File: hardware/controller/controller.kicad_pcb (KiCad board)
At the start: 4 copper layers, 80 x 100 mm, 70 parts, among them J1 TYPE-C 16PLT-H10.0, J2 TYPE-C 16PLT-H10.0, SW1 EVP-ASAC1A, SW2 CL-SB-13A-02T, SW3 EVP-ASAC1A, SW4 EVP-ASAC1A, SW5 EVP-ASAC1A, SW6 EVP-ASAC1A, U1 ZX-PM2.54-1-16PY, U10 XDJK-0051-025, U2 ZX-PM2.54-1-16PY, U3 ZX-PM2.54-1-16PY, U4 ZX-PM2.54-1-16PY, U5 SN74LVC1T45DBV, U6 SN74LVC1T45DBV, U7 EA8212HT6R, U8 EA8212HT6R, U9 EA8212HT6R

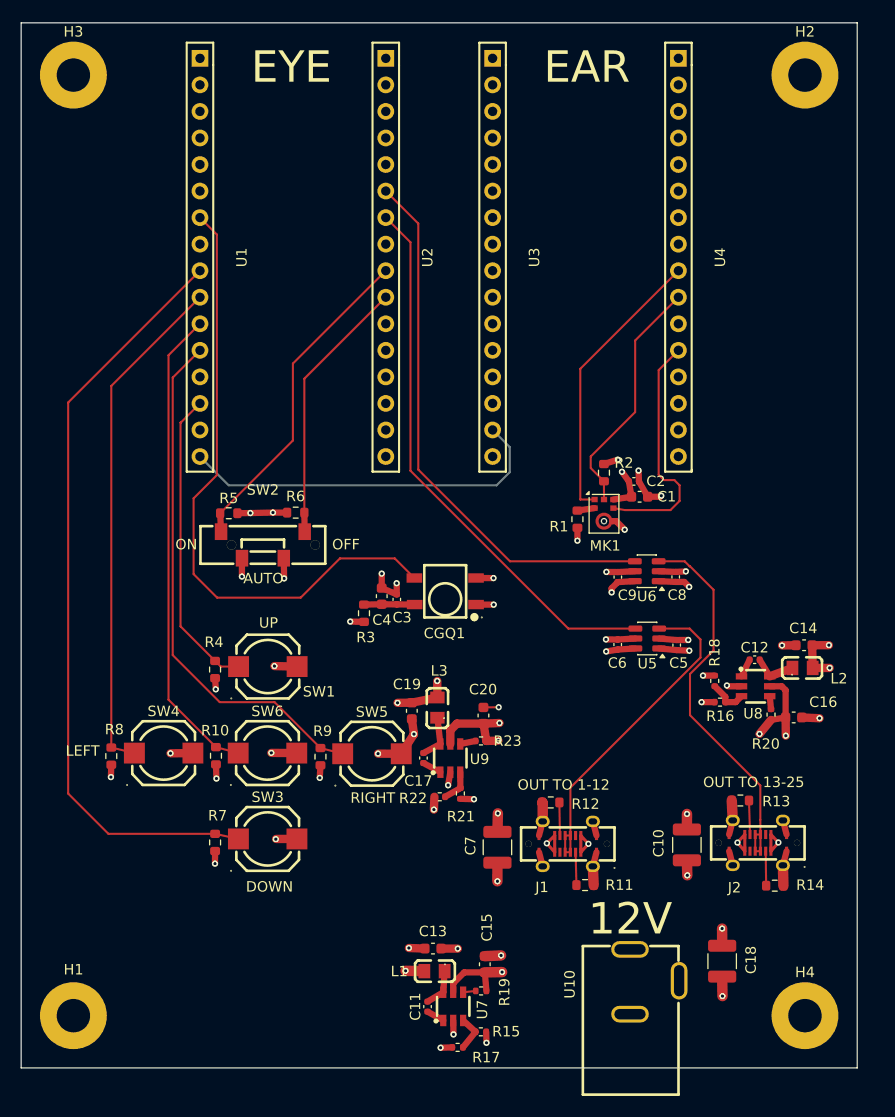
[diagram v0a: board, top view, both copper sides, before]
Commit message: updates to schematic based on feedback
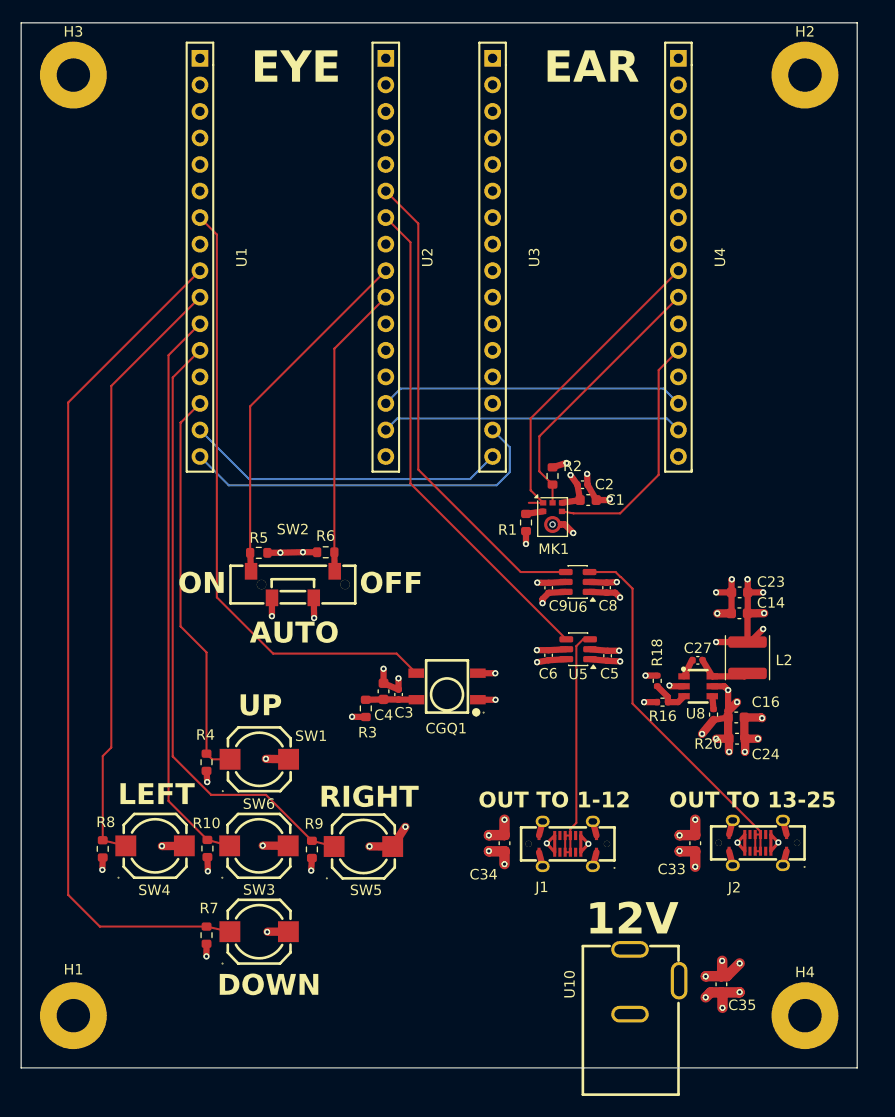
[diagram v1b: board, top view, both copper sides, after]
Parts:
- removed C10, C18, C7: 47µF, Capacitor_SMD:C_1210_3225Metric
- removed C11, C12, C17: 100nF, Capacitor_SMD:C_0402_1005Metric
- removed C13, C15, C19, C20: 10µF, Capacitor_SMD:C_0603_1608Metric
- removed L1, L3: MGFL2012F2R2MT-LF, easyeda2kicad:L0805
- removed R11, R12, R13, R14: 5.1kΩ, Resistor_SMD:R_0603_1608Metric
- removed R15, R19, R21, R23: 100kΩ, Resistor_SMD:R_0402_1005Metric
- removed R17: 732kΩ, Resistor_SMD:R_0402_1005Metric
- removed R22: 453kΩ, Resistor_SMD:R_0402_1005Metric
- removed U7, U9: EA8212HT6R, easyeda2kicad:SOT-23-6_L2.9-W1.6-P0.95-LS2.8-BR
- added C23: 10µF, Capacitor_SMD:C_0603_1608Metric, F.Cu at (177.2, 109.5)
- added C24: 10µF, Capacitor_SMD:C_0603_1608Metric, F.Cu at (177.0, 123.5)
- added C27: 33nF, Capacitor_SMD:C_0402_1005Metric, F.Cu at (173.2, 116.0)
- added C33: 10µF, Capacitor_SMD:C_0603_1608Metric, F.Cu at (173.0, 133.5)
- added C34: 10µF, Capacitor_SMD:C_0603_1608Metric, F.Cu at (154.8, 133.5)
- added C35: 10µF, Capacitor_SMD:C_0603_1608Metric, F.Cu at (175.5, 147.0)
- L2: value MGFL2012F2R2MT-LF -> 4.7uH; footprint easyeda2kicad:L0805 -> Inductor_SMD:L_Changjiang_FNR4030S
- moved C3 9.11 mm to (144.6, 119.3)
- moved CGQ1 9.11 mm to (149.2, 118.5)
- moved R3 9.11 mm to (141.5, 120.6)
- moved C4 9.11 mm to (143.2, 119.0)
- moved R8 8.91 mm to (116.3, 134.0)
- moved R4 8.91 mm to (126.2, 125.8)
- moved R7 8.91 mm to (126.2, 142.3)
- moved SW1 8.91 mm to (131.3, 125.5)
- moved SW3 8.91 mm to (131.3, 142.0)
- moved SW5 8.91 mm to (141.2, 133.8)
- moved SW6 8.91 mm to (131.2, 133.8)
- moved SW4 8.91 mm to (121.3, 133.8)
- moved R10 8.91 mm to (126.3, 134.0)
- moved R9 8.91 mm to (136.3, 134.1)
- moved C14 6.90 mm to (177.2, 111.5)
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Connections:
- J1 pad A5: Net-(J1-CC1) -> unconnected-(J1-CC1-PadA5)
- J1 pad B5: Net-(J1-CC2) -> unconnected-(J1-CC2-PadB5)
- J2 pad A5: Net-(J2-CC1) -> unconnected-(J2-CC1-PadA5)
- J2 pad B5: Net-(J2-CC2) -> unconnected-(J2-CC2-PadB5)
- U1 pad 15: unconnected-(U1-Pad15) -> /EYE_TO_EAR_FBK
- U2 pad 14: unconnected-(U2-Pad14) -> /BACKUP1
- U2 pad 15: unconnected-(U2-Pad15) -> /BACKUP2
- U2 pad 2: +5V -> +4V
- U3 pad 16: unconnected-(U3-Pad16) -> /EYE_TO_EAR_FBK
- U4 pad 14: unconnected-(U4-Pad14) -> /BACKUP1
- U4 pad 15: unconnected-(U4-Pad15) -> /BACKUP2
- U4 pad 2: +5V -> +4V
- U4 pad 5: unconnected-(U4-Pad5) -> +3.3V
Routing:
- net /EYE_TO_EAR_FBK: track 0.00 -> 30.8 mm
- net /BACKUP1: track 0.00 -> 29.2 mm
- net /BACKUP2: track 0.00 -> 28.9 mm
- net BTN LEFT: track 48.9 -> 58.1 mm
- net +4V: track 12.5 -> 21.2 mm, vias 5 -> 8
- net BTN RIGHT: track 50.3 -> 58.8 mm
- net BTN CENTER: track 45.8 -> 54.4 mm
- net BTN UP: track 29.3 -> 37.8 mm
- net BTN DOWN: track 73.2 -> 81.7 mm
- net SHIFTED_LED_DATA_1: track 32.5 -> 24.1 mm
- net +3.3V: track 26.0 -> 19.3 mm, vias 13 -> 10
- net LED DATA_2: track 52.3 -> 46.1 mm
- net +12V: track 45.9 -> 40.1 mm, vias 12 -> 16
- net LED DATA_1: track 53.0 -> 47.5 mm
- net +5V: track 4.44 -> 0.00 mm, vias 3 -> 0
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- removed copper zone on In2.Cu, net +5V

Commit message: fix up a few more things based on feedback
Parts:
- removed C4: 1µF, Capacitor_SMD:C_0603_1608Metric
- added C30: 4.7µF, Capacitor_SMD:C_0603_1608Metric, F.Cu at (143.2, 119.0)
- added R11: ~, Resistor_SMD:R_0603_1608Metric, F.Cu at (133.2, 112.2)
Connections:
- SW2 pad 2: GND -> Net-(R11-Pad1)
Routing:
- net Net-(R11-Pad1): track 0.00 -> 2.26 mm

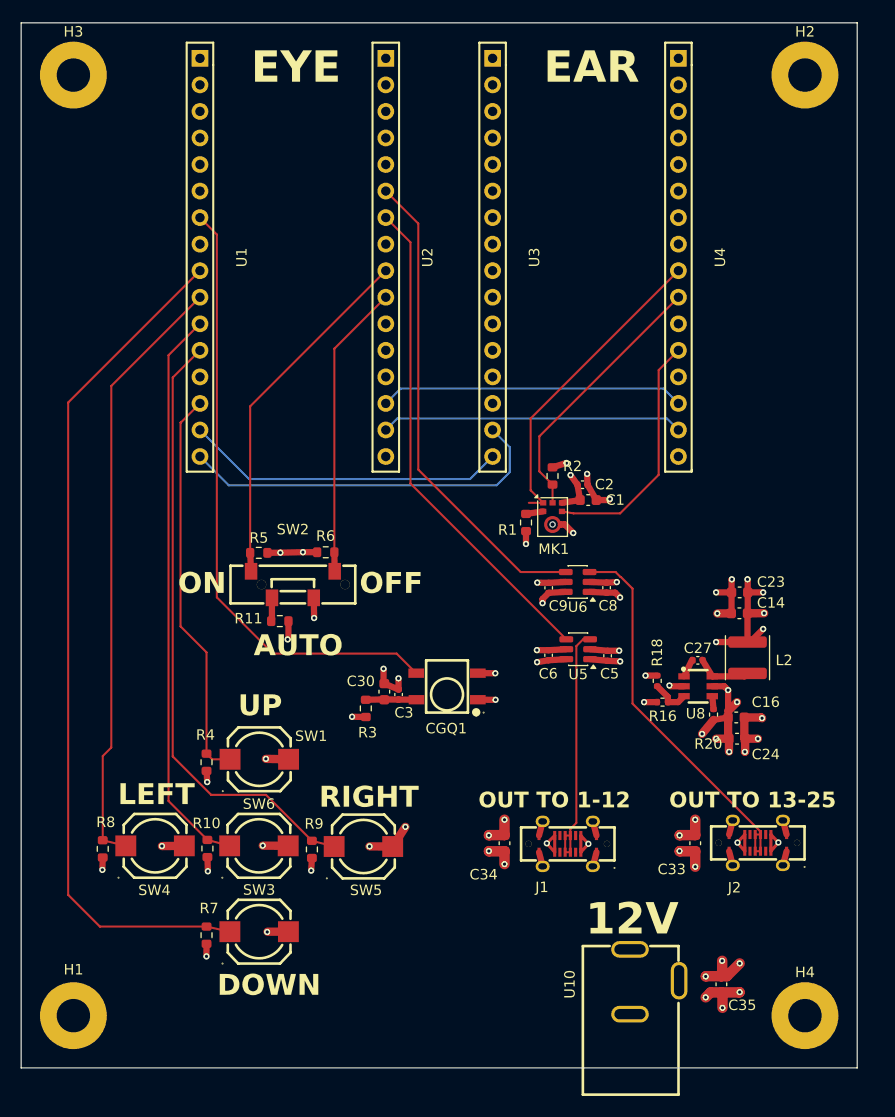
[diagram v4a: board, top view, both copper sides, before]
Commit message: working on updating controller board
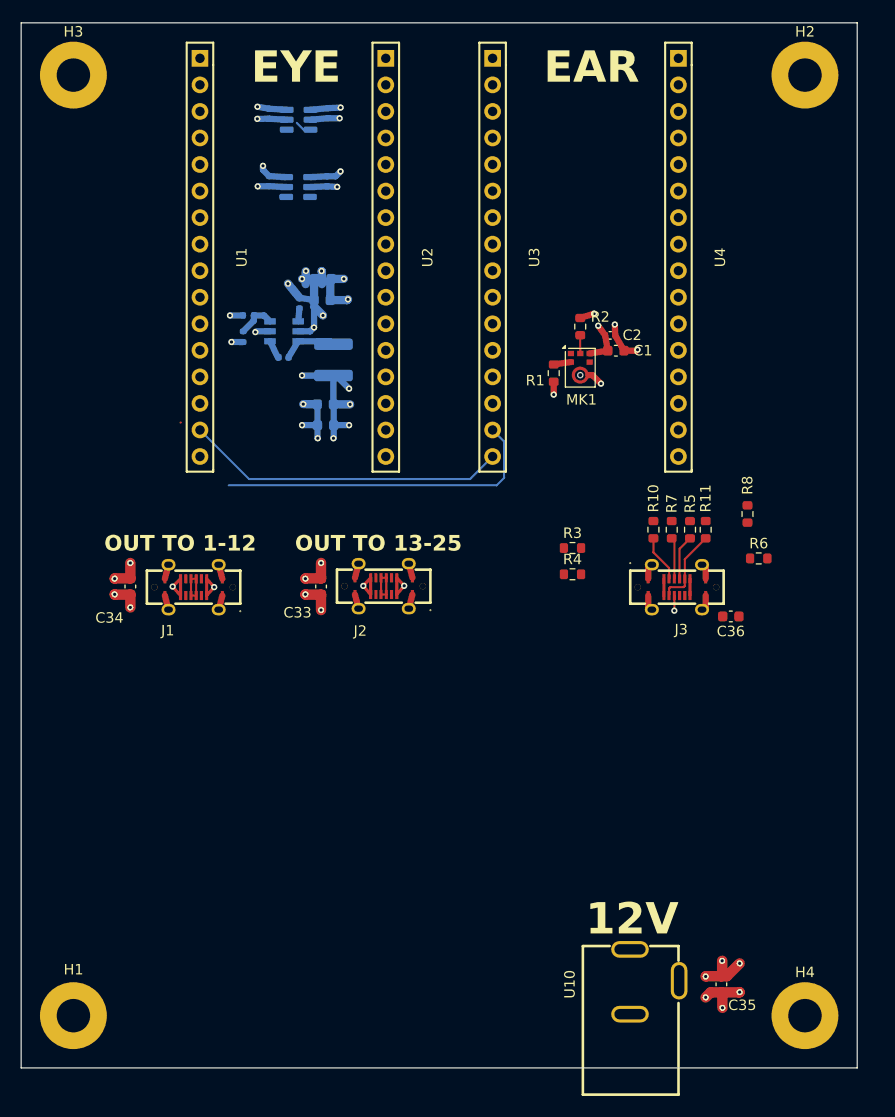
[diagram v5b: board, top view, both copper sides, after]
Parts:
- removed C3: 100nF, Capacitor_SMD:C_0402_1005Metric
- removed C30: 4.7µF, Capacitor_SMD:C_0603_1608Metric
- removed CGQ1: IRM-H638T/TR2, easyeda2kicad:SENSOR-SMD_IRM-H638T-TR2-TL
- removed R9: 10kΩ, Resistor_SMD:R_0603_1608Metric
- removed SW1, SW3, SW4, SW5, SW6: EVP-ASAC1A, easyeda2kicad:SW-SMD_PANASONIC_EVPASXXX
- removed SW2: CL-SB-13A-02T, easyeda2kicad:SW-SMD_CL-SB-13A-0X
- added C36: 10µF, Capacitor_SMD:C_0603_1608Metric, F.Cu at (176.4, 111.8)
- added J3: TYPE-C 16PLT-H10.0, easyeda2kicad:TYPE-C-SMD_USB4120-03-C, F.Cu at (171.2, 109.0)
- C14, C16, C23, C24, C27, C5, C6, C8, C9, L2, R16, R18, R20, U5, U6, U8: moved to B.Cu
- R10: value 10kΩ -> 1kΩ
- R11: value ~ -> 1kΩ
- R3: value 100Ω -> 10kΩ
- R5, R7: value 10kΩ -> 330Ω
- R6, R8: value 10kΩ -> 2.2kΩ
- moved R8 69.5 mm to (178.0, 102.0)
- moved C24 59.2 mm to (137.4, 79.5)
- moved R7 59.0 mm to (170.8, 103.5), turned to -90 degrees
- moved C5 58.4 mm to (137.9, 63.6), turned to 90 degrees
- moved C6 58.3 mm to (132.2, 63.7), turned to 90 degrees
- moved U5 57.3 mm to (135.0, 64.3)
- moved C16 56.3 mm to (137.3, 81.5)
- moved R20 55.9 mm to (135.1, 81.8), turned to 90 degrees
- moved R16 54.2 mm to (130.2, 83.0)
- moved R10 52.5 mm to (169.0, 103.5), turned to -90 degrees
- moved U8 52.2 mm to (133.7, 84.5)
- moved R18 51.5 mm to (129.7, 85.0), turned to -90 degrees
- moved C27 49.1 mm to (133.6, 87.0)
- moved L2 48.8 mm to (138.4, 87.2), turned to -90 degrees
- moved C9 47.2 mm to (132.2, 70.2), turned to 90 degrees
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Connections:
- R10 pad 1: +3.3V -> INT
- R10 pad 2: BTN CENTER -> Net-(J3-CC1)
- R11 pad 1: Net-(R11-Pad1) -> IR SENSOR DATA
- R11 pad 2: GND -> Net-(J3-SBU1)
- R3 pad 1: Net-(CGQ1-VCC) -> +3.3V
- R3 pad 2: +3.3V -> INT
- R4 pad 1: +3.3V -> IR SENSOR DATA
- R4 pad 2: BTN UP -> +3.3V
- R5 pad 1: SOUND REACTIVE ON -> Net-(J3-DN1)
- R5 pad 2: GND -> SCL
- R6 pad 1: SOUND REACTIVE OFF -> SCL
- R6 pad 2: GND -> +3.3V
- R7 pad 1: +3.3V -> SDA
- R7 pad 2: BTN DOWN -> Net-(J3-DP1)
- R8 pad 2: BTN LEFT -> SDA
- U1 pad 10: BTN LEFT -> unconnected-(U1-Pad10)
- U1 pad 11: BTN CENTER -> unconnected-(U1-Pad11)
- U1 pad 12: BTN RIGHT -> unconnected-(U1-Pad12)
- U1 pad 14: BTN UP -> unconnected-(U1-Pad14)
- U1 pad 9: BTN DOWN -> INT
- U2 pad 14: /BACKUP1 -> SCL
- U2 pad 15: /BACKUP2 -> SDA
- U4 pad 14: /BACKUP1 -> unconnected-(U4-Pad14)
- U4 pad 15: /BACKUP2 -> unconnected-(U4-Pad15)
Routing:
- net BTN DOWN: track 81.7 -> 0.00 mm
- net IR SENSOR DATA: track 59.1 -> 0.00 mm
- net BTN RIGHT: track 58.8 -> 0.00 mm
- net BTN LEFT: track 58.1 -> 0.00 mm
- net BTN CENTER: track 54.4 -> 0.00 mm
- net LED DATA_1: track 47.5 -> 0.00 mm
- net LED DATA_2: track 46.1 -> 0.00 mm
- net BTN UP: track 37.8 -> 0.00 mm
- net SOUND REACTIVE ON: track 34.1 -> 0.00 mm
- net SHIFTED_LED_DATA_2: track 37.6 -> 4.49 mm
- net MIC WS: track 29.9 -> 0.00 mm
- net /BACKUP1: track 29.2 -> 0.00 mm
- net /BACKUP2: track 28.9 -> 0.00 mm
- net SOUND REACTIVE OFF: track 28.3 -> 0.00 mm
- net MIC DATA OUTPUT: track 25.7 -> 1.74 mm
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- removed copper zone on In2.Cu, net +12V
- removed copper zone on In2.Cu, net +3.3V
- removed copper zone on In2.Cu, net +4V
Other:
- board text removed: "AUTO"
- board text removed: "DOWN"
- board text removed: "LEFT"
- board text removed: "OFF"
- board text removed: "ON"
- board text removed: "RIGHT"
- board text removed: "UP"

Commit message: revised controller board
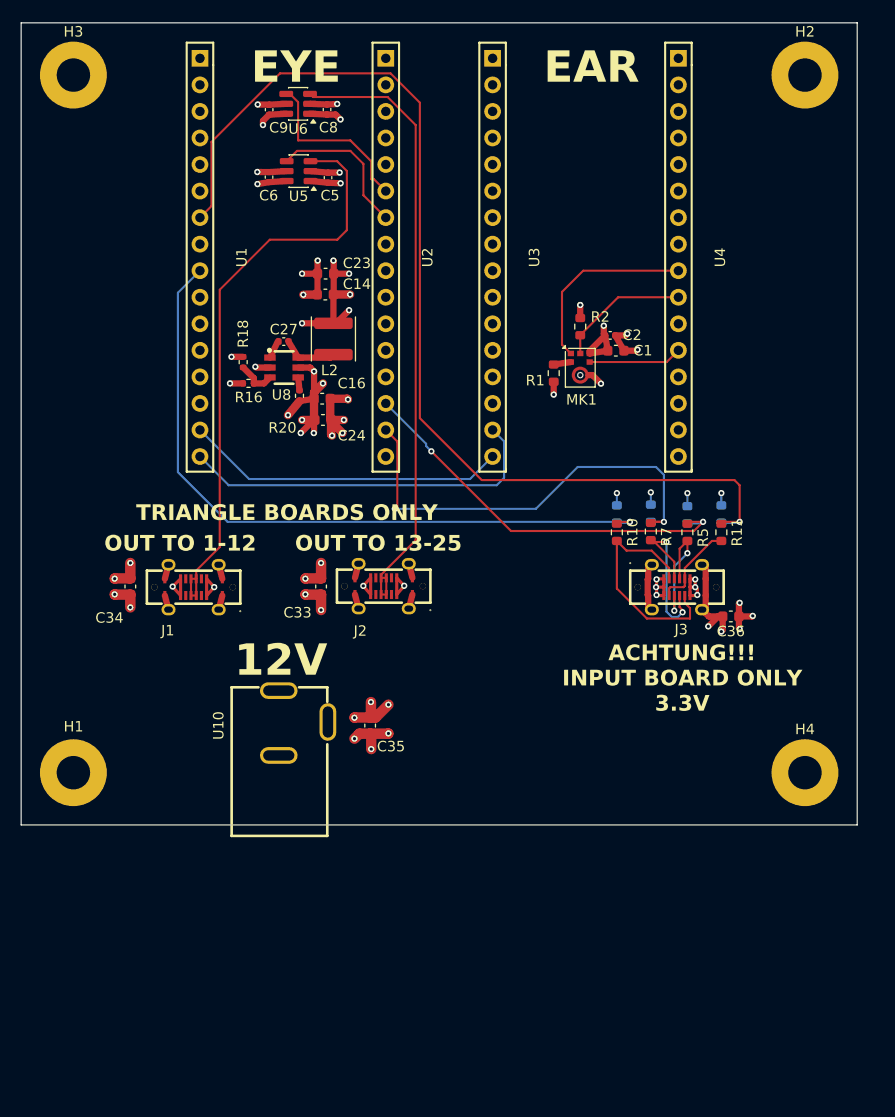
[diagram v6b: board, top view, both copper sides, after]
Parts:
- C14, C16, C23, C24, C27, C5, C6, C8, C9, L2, R16, R18, R20, U5, U6, U8: moved to F.Cu
- R3, R4, R6, R8: moved to B.Cu
- moved C35 41.7 mm to (141.9, 122.2)
- moved U10 41.7 mm to (135.5, 122.0)
- moved H1 23.2 mm to (113.5, 126.8)
- moved H4 23.2 mm to (183.5, 126.8)
- moved R4 15.4 mm to (175.5, 102.0), turned to 90 degrees
- moved C23 14.5 mm to (137.6, 79.0)
- moved C24 13.5 mm to (137.4, 93.0)
- moved C14 10.5 mm to (137.6, 81.0)
- moved C16 9.43 mm to (137.3, 91.0)
- moved R8 9.25 mm to (168.8, 101.9), turned to -90 degrees
- moved R20 8.88 mm to (135.1, 90.7), turned to -90 degrees
- moved R6 8.00 mm to (172.2, 102.1), turned to 90 degrees
- moved U6 7.96 mm to (135.0, 62.7)
- moved C8 6.87 mm to (137.8, 63.3), turned to -90 degrees
- moved C9 6.84 mm to (132.2, 63.3), turned to -90 degrees
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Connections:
- U2 pad 5: unconnected-(U2-Pad5) -> +3.3V
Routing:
- net IR SENSOR DATA: track 0.00 -> 101.8 mm, vias 0 -> 1
- net INT: track 0.00 -> 67.7 mm, vias 0 -> 1
- net SHIFTED_LED_DATA_2: track 4.49 -> 60.0 mm
- net SHIFTED_LED_DATA_1: track 5.78 -> 56.8 mm
- net SDA: track 0.00 -> 43.9 mm, vias 0 -> 2
- net SCL: track 0.00 -> 38.8 mm, vias 0 -> 2
- net MIC WS: track 0.00 -> 18.2 mm
- net +3.3V: track 13.3 -> 31.2 mm, vias 3 -> 16
- net Net-(J3-CC1): track 4.50 -> 22.3 mm
- net LED DATA_2: track 0.00 -> 16.2 mm
- net LED DATA_1: track 0.00 -> 14.3 mm
- net Net-(J3-DP1): track 3.98 -> 16.6 mm, vias 0 -> 2
- net GND: track 60.8 -> 72.8 mm, vias 23 -> 27
- net MIC DATA OUTPUT: track 1.74 -> 12.6 mm
- net MIC CLOCK: track 0.00 -> 8.95 mm
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- added copper zone on In2.Cu, net +12V
- added copper zone on In2.Cu, net +3.3V
- added copper zone on In2.Cu, net +4V
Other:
- board size 80 x 100 mm -> 80 x 76.8 mm
- board text added: "ACHTUNG!!! INPUT BOARD ONLY 3.3V"
- board text added: "TRIANGLE BOARDS ONLY"
